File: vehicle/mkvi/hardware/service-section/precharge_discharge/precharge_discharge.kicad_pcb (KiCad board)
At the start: 2 copper layers, 25.1 x 6.5 mm, 28 parts, among them J1 MicroFit_VT_5x1, J2 Automotive_M.2_Edge_Connector, K1 G2RG-2A-X_DC12, K2 3350-4275-126, Q1 SSM3K333R, U1 MCP6001, U2 MCP6001, U3 MCP6001

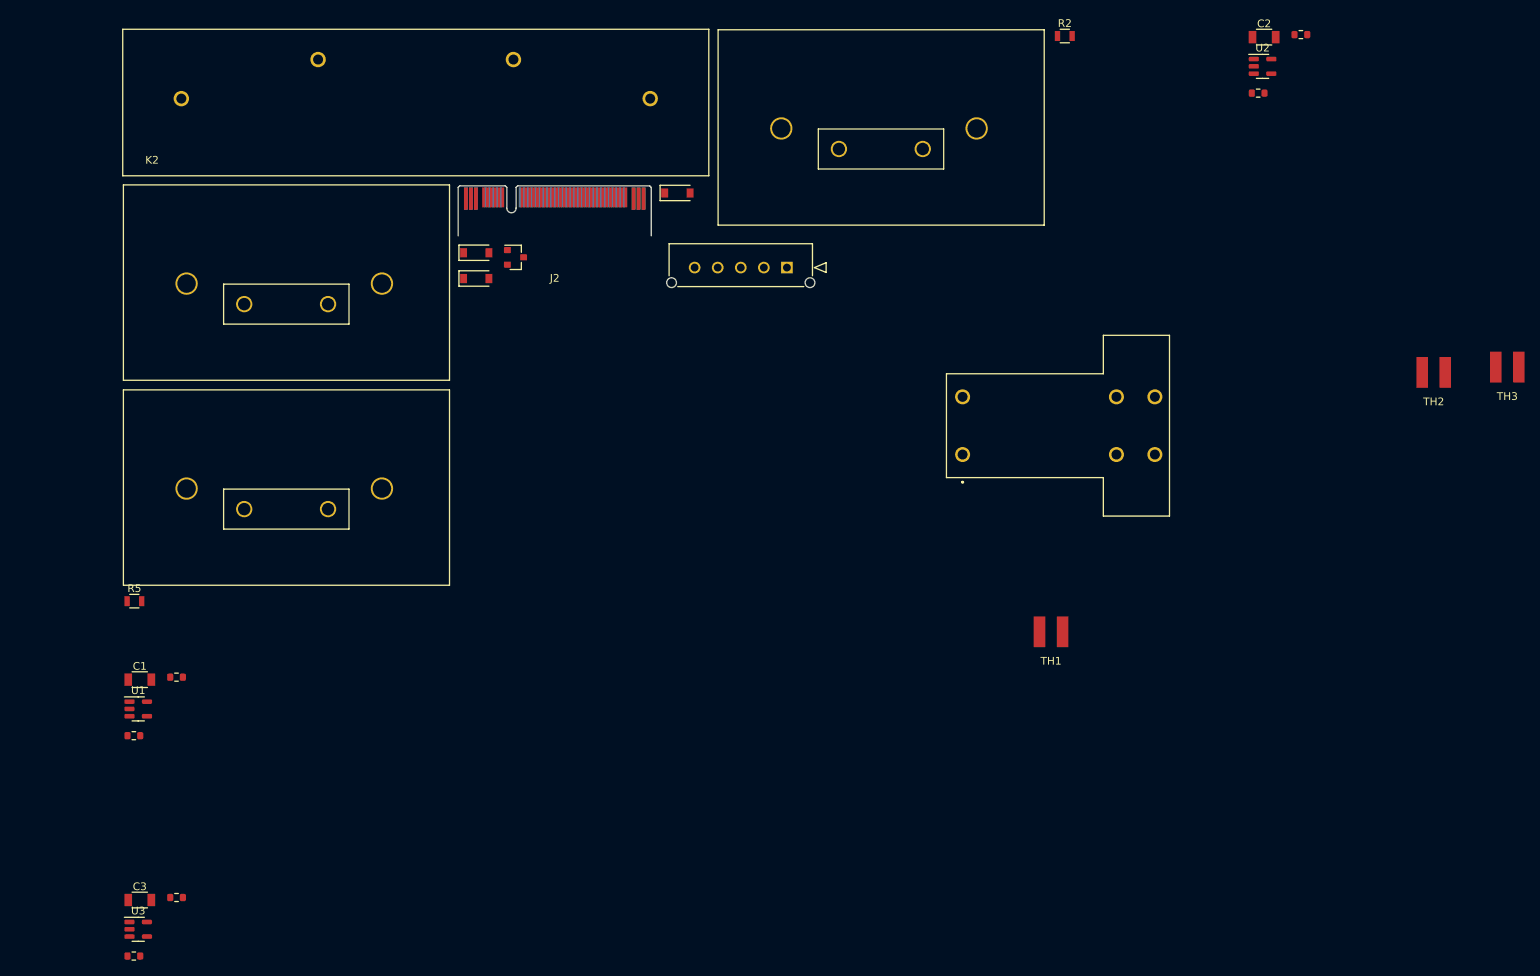
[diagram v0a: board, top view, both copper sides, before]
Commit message: V1. Precharge_Discharge PCB Layout
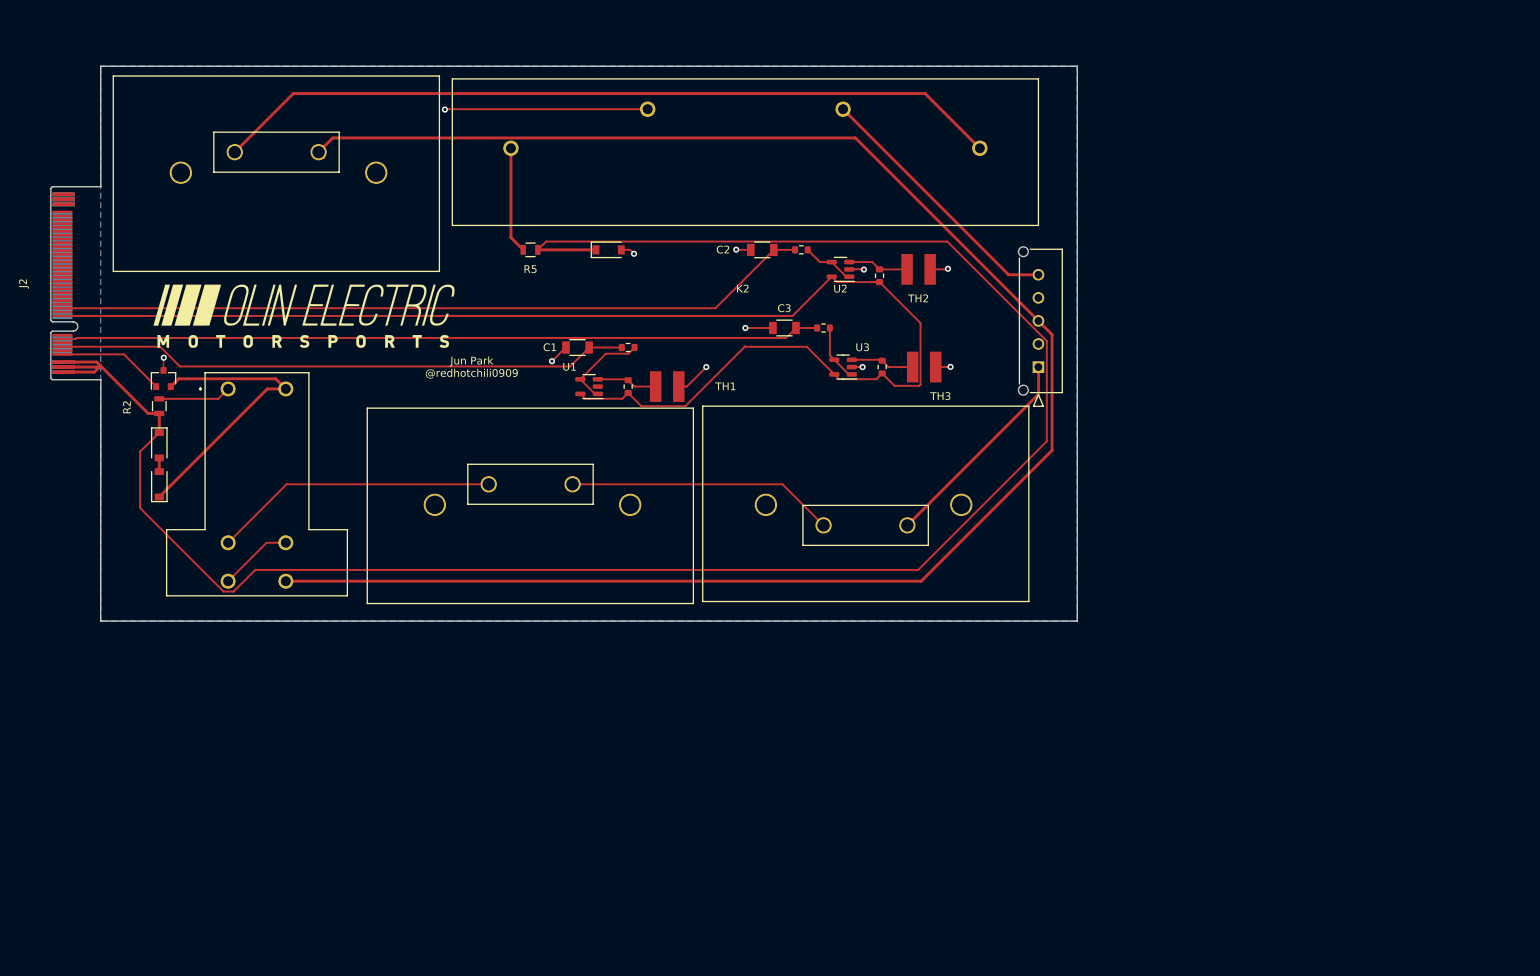
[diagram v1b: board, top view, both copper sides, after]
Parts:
- added G***: LOGO, footprints:Logo_Large, F.Cu at (92.5, 95.0)
- moved R2 127.2 mm to (73.7, 106.7), turned to -90 degrees
- moved R12 121.3 mm to (160.0, 96.5)
- moved U3 117.2 mm to (162.6, 101.6), turned to 180 degrees
- moved R11 114.8 mm to (167.6, 101.6), turned to 90 degrees
- moved C3 112.1 mm to (154.9, 96.5), turned to 180 degrees
- moved K1 95.9 mm to (82.6, 104.4), turned to -90 degrees
- moved R8 81.7 mm to (134.6, 99.1)
- moved TH3 75.8 mm to (173.1, 101.6)
- moved R4 75.3 mm to (160.0, 122.2)
- moved D1 74.9 mm to (73.7, 111.8), turned to -90 degrees
- moved U1 72.1 mm to (129.5, 104.1), turned to 180 degrees
- moved C1 71.4 mm to (128.0, 99.1), turned to 180 degrees
- moved C2 70.9 mm to (152.1, 86.4), turned to 180 degrees
- moved R7 69.8 mm to (134.6, 104.1), turned to 90 degrees
- moved R5 68.8 mm to (121.9, 86.4)
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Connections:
- J2 pad 10: /TEMP_SENSE_PRECHARGE2 -> +5V
- J2 pad 12: +5V -> /TEMP_SENSE_DISCHARGE
- J2 pad 6: /TEMP_SENSE_DISCHARGE -> /TEMP_SENSE_PRECHARGE2
- K2 pad 2: /HV_TS- -> unconnected-(K2-Pad2)
- R2 pad 1: Net-(K1-Pad1) -> /FINAL_SHUTDOWN
- R2 pad 2: /FINAL_SHUTDOWN -> Net-(K1-Pad1)
- R5 pad 1: Net-(K2-Pad4) -> /FINAL_SHUTDOWN
- R5 pad 2: /FINAL_SHUTDOWN -> Net-(K2-Pad4)
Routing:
- net /FINAL_SHUTDOWN: track 0.00 -> 261.4 mm
- net /HV_TS+: track 0.00 -> 229.5 mm
- net +5V: track 0.00 -> 175.8 mm
- net Net-(K2-Pad1): track 0.00 -> 103.0 mm
- net /TEMP_SENSE_PRECHARGE1: track 0.00 -> 98.7 mm
- net /TEMP_SENSE_DISCHARGE: track 0.00 -> 98.7 mm
- net /TEMP_SENSE_PRECHARGE2: track 0.00 -> 74.8 mm
- net GND: track 0.00 -> 50.2 mm, vias 0 -> 11
- net /PRECHARGE_COIL: track 0.00 -> 38.2 mm
- net Net-(K1-Pad3): track 0.00 -> 37.0 mm
- net Net-(R3-Pad1): track 0.00 -> 34.8 mm
- net /HV_TS-: track 0.00 -> 34.3 mm
- net /HV_BAT+: track 0.00 -> 27.7 mm
- net /PRECHARGE_LSD: track 0.00 -> 13.9 mm
- net Net-(K2-Pad4): track 0.00 -> 13.9 mm
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- added copper zone on B.Cu, net GND
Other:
- board size 25.1 x 6.5 mm -> 127 x 72.1 mm
- board text added: "Jun Park @redhotchili0909"

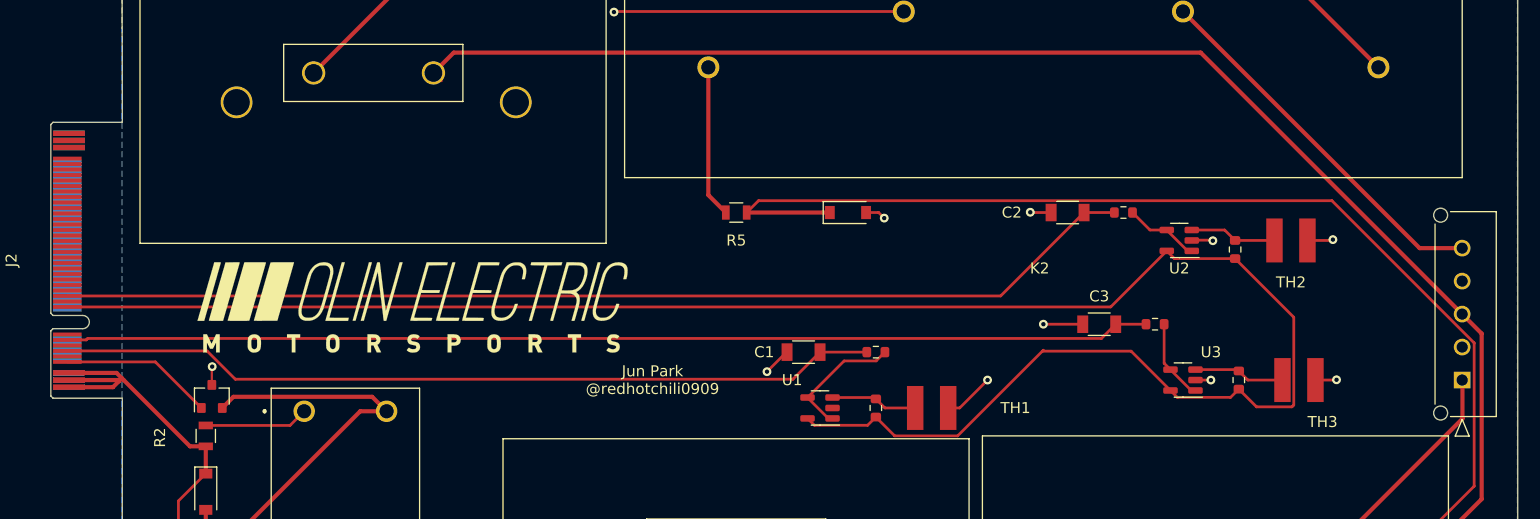
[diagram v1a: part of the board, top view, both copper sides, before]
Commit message: V2. Precharge_Discharge PCB Layout
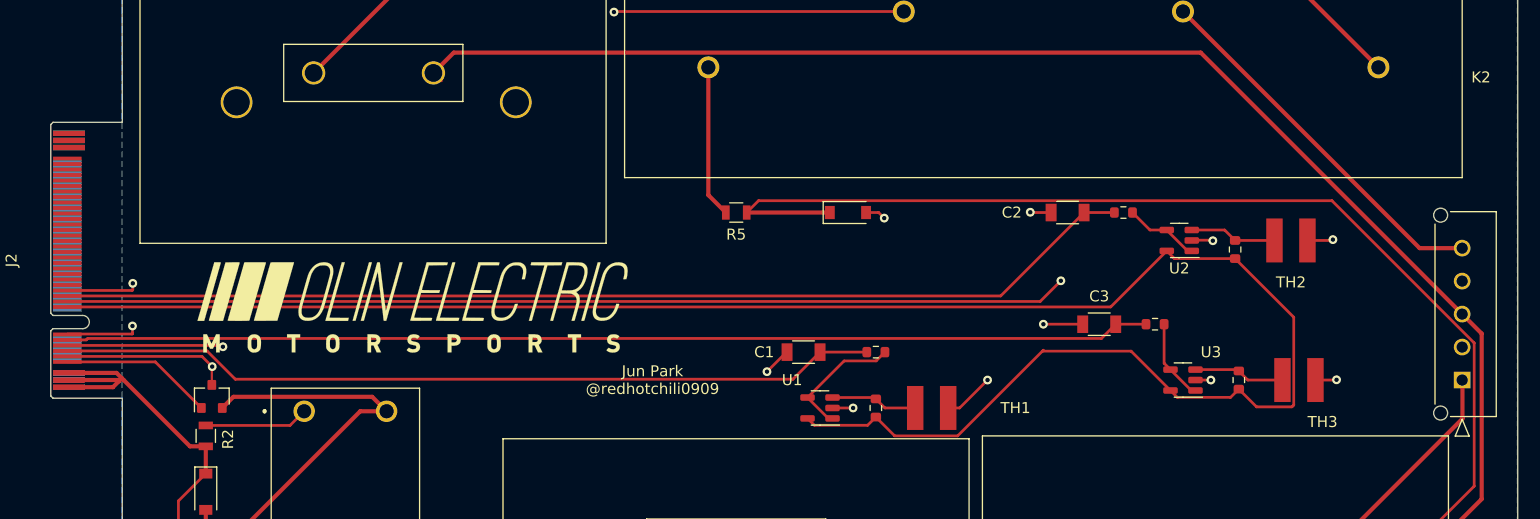
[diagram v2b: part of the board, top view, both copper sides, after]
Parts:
- turned R2 to 90 degrees
- turned R5 to 180 degrees
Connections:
- K2 pad 2: unconnected-(K2-Pad2) -> /HV_TS-
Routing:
- net GND: track 50.2 -> 184.3 mm, vias 11 -> 16
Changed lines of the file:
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@@
   (net 85 "Net-(R12-Pad2)")
   (net 86 "Net-(K1-Pad4)")
-  (net 87 "unconnected-(K2-Pad2)")
   (footprint "footprints:Thermistor" (layer "F.Cu")
     (at 173.11 101.6)
@@
   )
   (footprint "footprints:R_0805_OEM" (layer "F.Cu")
-    (at 121.92 86.36)
+    (at 121.92 86.36 180)
     (descr "Resistor SMD 0805, reflow soldering, Vishay (see dcrcw.pdf)")
     (tags "resistor 0805")
@@
     (property "Sheetname" "")
     (attr smd)
-    (fp_text reference "R5" (at 0 2.54) (layer "F.SilkS")
+    (fp_text reference "R5" (at 0.01 -2) (layer "F.SilkS")
       (effects (font (size 1 1) (thickness 0.15)))
     )
@@
     (fp_line (start 1 0.62) (end -1 0.62) (layer "F.Fab") (width 0.1))
     (fp_line (start -1 -0.62) (end 1 -0.62) (layer "F.Fab") (width 0.1))
-    (pad "1" smd rect locked (at -0.95 0) (size 0.7 1.3) (layers "F.Cu" "F.Paste" "F.Mask")
+    (pad "1" smd rect locked (at -0.95 0 180) (size 0.7 1.3) (layers "F.Cu" "F.Paste" "F.Mask")
       (net 5 "/FINAL_SHUTDOWN") (pintype "passive"))
-    (pad "2" smd rect locked (at 0.95 0) (size 0.7 1.3) (layers "F.Cu" "F.Paste" "F.Mask")
+    (pad "2" smd rect locked (at 0.95 0 180) (size 0.7 1.3) (layers "F.Cu" "F.Paste" "F.Mask")
       (net 76 "Net-(K2-Pad4)") (pintype "passive"))
     (model "${OEM_DIR}/parts/3DModels/R_0805_OEM/res0805.step"
@@
       (effects (font (size 1 1) (thickness 0.15)))
     )
-    (fp_text user "${REFERENCE}" (at -5.08 0) (layer "F.Fab")
+    (fp_text user "${REFERENCE}" (at -0.23 3.74) (layer "F.Fab")
       (effects (font (size 1 1) (thickness 0.15)))
     )
@@
     (property "Sheetname" "")
     (attr through_hole)
-    (fp_text reference "K2" (at 33.9525 10.795) (layer "F.SilkS")
+    (fp_text reference "K2" (at 74.1 -6.585) (layer "F.SilkS")
       (effects (font (size 1 1) (thickness 0.15)))
     )
-    (fp_text value "3350-4275-126" (at 44.1125 10.795) (layer "F.Fab")
+    (fp_text value "3350-4275-126" (at 2.46 3.565) (layer "F.Fab")
       (effects (font (size 1 1) (thickness 0.15)))
     )
@@
       (net 75 "Net-(K2-Pad1)") (pintype "passive"))
     (pad "2" thru_hole circle (at 46.99 -12.573) (size 2 2) (drill 1.3) (layers *.Cu *.Mask)
-      (net 87 "unconnected-(K2-Pad2)") (pintype "passive"))
+      (net 12 "/HV_TS-") (pintype "passive"))
     (pad "3" thru_hole circle (at 21.59 -12.573) (size 2 2) (drill 1.3) (layers *.Cu *.Mask)
       (net 2 "GND") (pinfunction "-") (pintype "passive"))
@@
   )
   (footprint "footprints:R_0805_OEM" (layer "F.Cu")
-    (at 73.66 106.68 -90)
+    (at 73.66 106.68 90)
     (descr "Resistor SMD 0805, reflow soldering, Vishay (see dcrcw.pdf)")
     (tags "resistor 0805")
@@
     (property "Sheetname" "")
     (attr smd)
-    (fp_text reference "R2" (at 0.1524 4.1656 90) (layer "F.SilkS")
+    (fp_text reference "R2" (at -0.3 2.02 90) (layer "F.SilkS")
       (effects (font (size 1 1) (thickness 0.15)))
     )
@@
     (fp_line (start 1 0.62) (end -1 0.62) (layer "F.Fab") (width 0.1))
     (fp_line (start 1 -0.62) (end 1 0.62) (layer "F.Fab") (width 0.1))
-    (pad "1" smd rect locked (at -0.95 0 270) (size 0.7 1.3) (layers "F.Cu" "F.Paste" "F.Mask")
+    (pad "1" smd rect locked (at -0.95 0 90) (size 0.7 1.3) (layers "F.Cu" "F.Paste" "F.Mask")
       (net 5 "/FINAL_SHUTDOWN") (pintype "passive"))
-    (pad "2" smd rect locked (at 0.95 0 270) (size 0.7 1.3) (layers "F.Cu" "F.Paste" "F.Mask")
+    (pad "2" smd rect locked (at 0.95 0 90) (size 0.7 1.3) (layers "F.Cu" "F.Paste" "F.Mask")
       (net 77 "Net-(K1-Pad1)") (pintype "passive"))
     (model "${OEM_DIR}/parts/3DModels/R_0805_OEM/res0805.step"
@@
   (segment (start 150.5625 86.36) (end 148.6916 86.36) (width 0.254) (layer "F.Cu") (net 2))
   (segment (start 174.61 101.6) (end 176.5046 101.6) (width 0.254) (layer "F.Cu") (net 2))
+  (segment (start 61.064 93.45) (end 66.96 93.45) (width 0.25) (layer "F.Cu") (net 2))
   (segment (start 142.24 104.14) (end 144.78 101.6) (width 0.25) (layer "F.Cu") (net 2))
+  (segment (start 67.02 93.39) (end 67.02 92.8) (width 0.25) (layer "F.Cu") (net 2))
+  (segment (start 130.6775 104.14) (end 132.31 104.14) (width 0.25) (layer "F.Cu") (net 2))
   (segment (start 137.16 68.072) (end 110.8456 68.072) (width 0.254) (layer "F.Cu") (net 2))
   (segment (start 163.36 88.9) (end 163.4744 88.9) (width 0.254) (layer "F.Cu") (net 2))
@@
   (segment (start 74.21 100.415) (end 74.2442 100.3808) (width 0.2) (layer "F.Cu") (net 2))
   (segment (start 141.2 104.14) (end 142.24 104.14) (width 0.25) (layer "F.Cu") (net 2))
+  (segment (start 66.99 97.3834) (end 66.99 96.68) (width 0.25) (layer "F.Cu") (net 2))
+  (segment (start 66.96 97.4134) (end 66.99 97.3834) (width 0.25) (layer "F.Cu") (net 2))
   (segment (start 173.8825 88.9) (end 176.1236 88.9) (width 0.254) (layer "F.Cu") (net 2))
   (segment (start 176.5046 101.6) (end 176.53 101.5746) (width 0.254) (layer "F.Cu") (net 2))
   (segment (start 163.6975 101.6) (end 165.1 101.6) (width 0.25) (layer "F.Cu") (net 2))
+  (segment (start 132.34 104.17) (end 132.52 104.17) (width 0.25) (layer "F.Cu") (net 2))
+  (segment (start 132.52 104.17) (end 132.55 104.14) (width 0.25) (layer "F.Cu") (net 2))
   (segment (start 148.6916 86.36) (end 148.6662 86.3346) (width 0.254) (layer "F.Cu") (net 2))
   (segment (start 134.874 86.36) (end 135.382 86.868) (width 0.25) (layer "F.Cu") (net 2))
+  (segment (start 73.3134 99.45) (end 74.2442 100.3808) (width 0.25) (layer "F.Cu") (net 2))
+  (segment (start 75.1 98.45) (end 75.22 98.57) (width 0.25) (layer "F.Cu") (net 2))
+  (segment (start 149.57 94.45) (end 151.45 92.57) (width 0.25) (layer "F.Cu") (net 2))
   (segment (start 133.73 86.36) (end 134.874 86.36) (width 0.25) (layer "F.Cu") (net 2))
   (segment (start 110.8456 68.072) (end 110.7948 68.1228) (width 0.254) (layer "F.Cu") (net 2))
   (segment (start 176.1236 88.9) (end 176.1998 88.8238) (width 0.254) (layer "F.Cu") (net 2))
+  (segment (start 66.96 93.45) (end 67.02 93.39) (width 0.25) (layer "F.Cu") (net 2))
+  (segment (start 61.064 97.45) (end 61.1006 97.4134) (width 0.25) (layer "F.Cu") (net 2))
+  (segment (start 132.31 104.14) (end 132.34 104.17) (width 0.25) (layer "F.Cu") (net 2))
   (segment (start 74.21 102.04) (end 74.21 100.415) (width 0.2) (layer "F.Cu") (net 2))
   (segment (start 163.4744 88.9) (end 163.4998 88.8746) (width 0.254) (layer "F.Cu") (net 2))
   (segment (start 165.227 88.8746) (end 165.2778 88.9254) (width 0.254) (layer "F.Cu") (net 2))
+  (segment (start 61.064 98.45) (end 75.1 98.45) (width 0.25) (layer "F.Cu") (net 2))
   (segment (start 126.54 99.06) (end 126.492 99.06) (width 0.25) (layer "F.Cu") (net 2))
   (segment (start 126.492 99.06) (end 124.714 100.838) (width 0.25) (layer "F.Cu") (net 2))
+  (segment (start 61.064 94.45) (end 149.57 94.45) (width 0.25) (layer "F.Cu") (net 2))
+  (segment (start 61.1006 97.4134) (end 66.96 97.4134) (width 0.25) (layer "F.Cu") (net 2))
   (segment (start 153.44 96.52) (end 149.86 96.52) (width 0.25) (layer "F.Cu") (net 2))
+  (segment (start 61.064 99.45) (end 73.3134 99.45) (width 0.25) (layer "F.Cu") (net 2))
   (via (at 165.1 101.6) (size 0.8) (drill 0.4) (layers "F.Cu" "B.Cu") (net 2))
   (via (at 176.53 101.5746) (size 0.8) (drill 0.4) (layers "F.Cu" "B.Cu") (net 2))
@@
   (via (at 148.6662 86.3346) (size 0.8) (drill 0.4) (layers "F.Cu" "B.Cu") (net 2))
   (via (at 110.7948 68.1228) (size 0.8) (drill 0.4) (layers "F.Cu" "B.Cu") (net 2))
+  (via (at 75.22 98.57) (size 0.8) (drill 0.4) (layers "F.Cu" "B.Cu") (net 2))
   (via (at 144.78 101.6) (size 0.8) (drill 0.4) (layers "F.Cu" "B.Cu") (net 2))
   (via (at 124.714 100.838) (size 0.8) (drill 0.4) (layers "F.Cu" "B.Cu") (net 2))
   (via (at 176.1998 88.8238) (size 0.8) (drill 0.4) (layers "F.Cu" "B.Cu") (net 2))
+  (via (at 132.55 104.14) (size 0.8) (drill 0.4) (layers "F.Cu" "B.Cu") (net 2))
+  (via (at 66.99 96.68) (size 0.8) (drill 0.4) (layers "F.Cu" "B.Cu") (net 2))
   (via (at 149.86 96.52) (size 0.8) (drill 0.4) (layers "F.Cu" "B.Cu") (net 2))
+  (via (at 151.45 92.57) (size 0.8) (drill 0.4) (layers "F.Cu" "B.Cu") (net 2))
   (via (at 135.382 86.868) (size 0.8) (drill 0.4) (layers "F.Cu" "B.Cu") (net 2))
+  (via (at 67.02 92.8) (size 0.8) (drill 0.4) (layers "F.Cu" "B.Cu") (net 2))
   (segment (start 153.5625 86.36) (end 153.5625 86.66) (width 0.25) (layer "F.Cu") (net 3))
   (segment (start 145.9725 93.95) (end 61.064 93.95) (width 0.254) (layer "F.Cu") (net 3))
